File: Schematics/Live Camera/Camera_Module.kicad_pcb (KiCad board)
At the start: 2 copper layers, 69.5 x 60 mm, 90 parts, among them J1 Stack Male Edge Connector, J2 SWD_01x04_Pin, J3 USB_C_Female_USB2_Small, J4 Therm_In, J5 VTX, J6 RunCam6, J7 VTX_BATT_IN, J8 VTX_BATT_SWITCH, Q2 AO3401A, Q3 AO3400A, Q4 AO3400A, Q5 AO3401A, Q6 AO3401A, SW1 SW_STM_RESET, SW2 SW_STM_BOOT_MODE, U1 LM66100DCKR, U10 AMS1117-3.3, U11 CP2102N-Axx-xQFN28, U2 TPM8837C-SO1R, U3 STM32F103CBT6, U5 LM66100DCKR, U6 LM66100DCKR, U7 ISO1042BDWVR, U8 W25Q128JVS, Y1 X322516MMB4SI

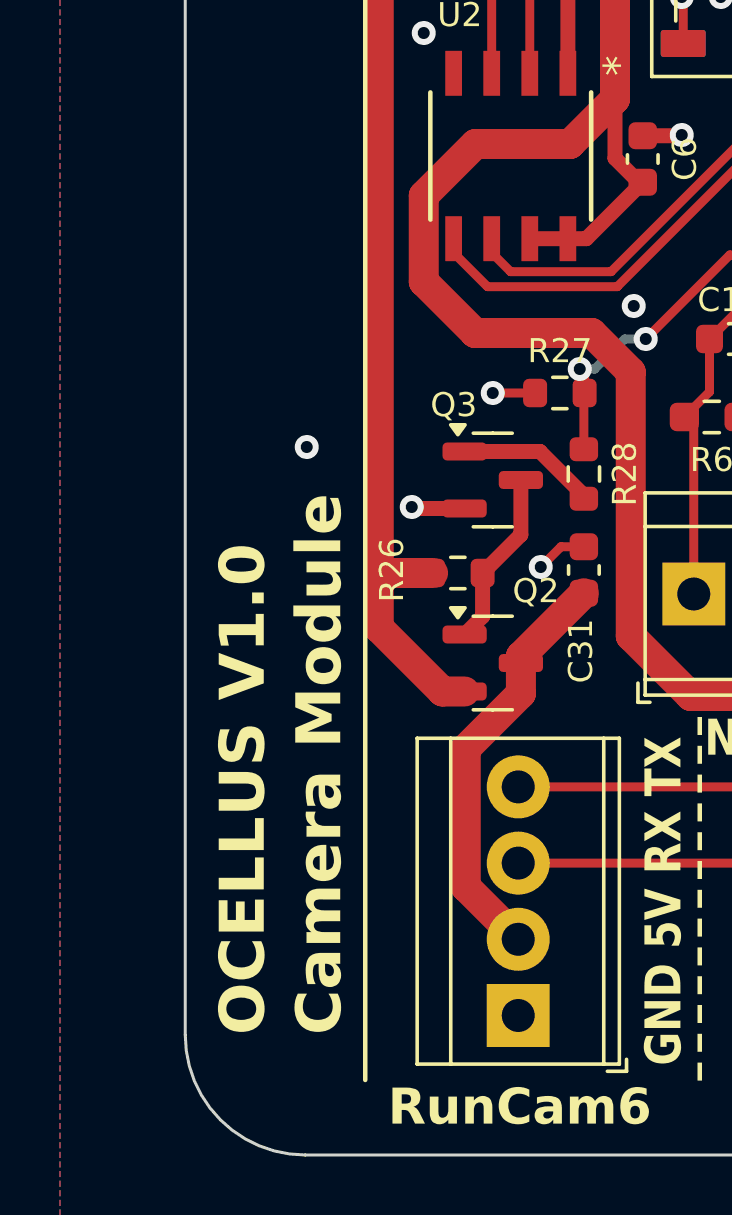
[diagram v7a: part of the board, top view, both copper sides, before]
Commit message: Final silkscreen update
Also reverted JLCPCB fields back to LCSC fields for JLCPCB export plugin purposes.
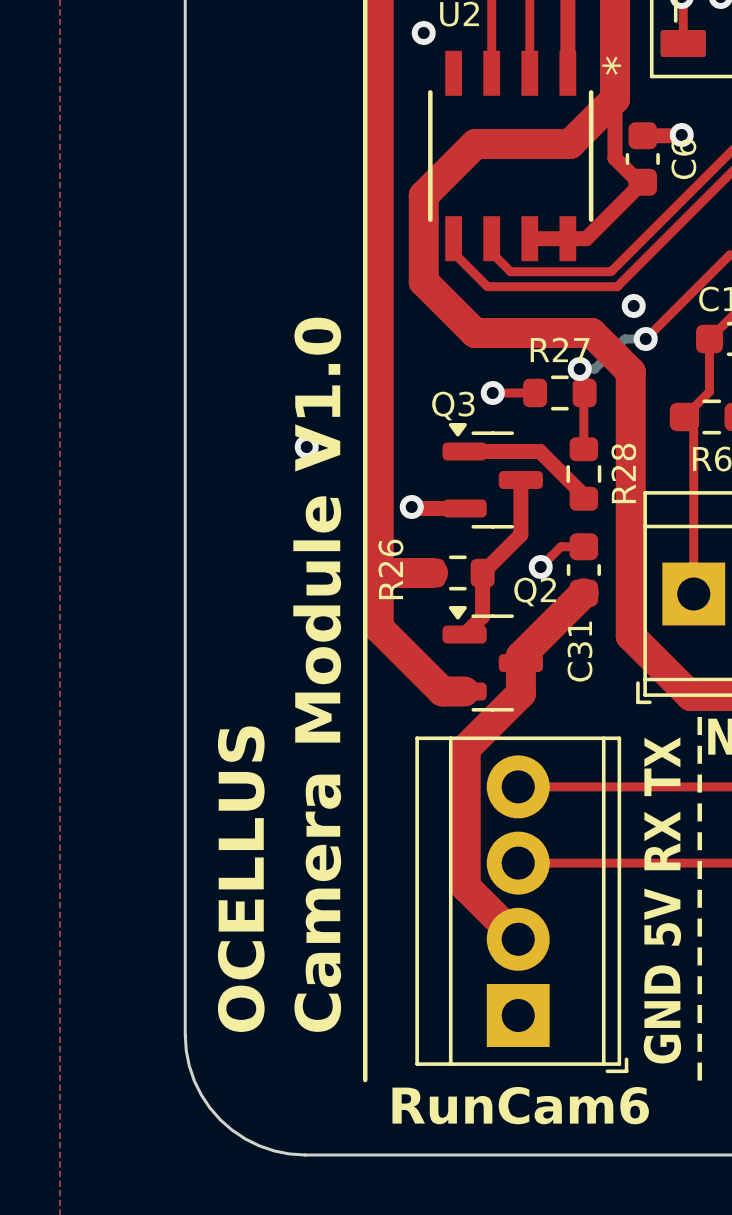
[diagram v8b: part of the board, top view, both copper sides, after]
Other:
- board text added: "Camera Module V1.0"
- board text added: "Camera Module V1.0 QRET Mar 2025 Ethan Toste Kennan Bays Noah Del Rizzo Fedor Kim"
- board text added: "OCELLUS"
- board text removed: "Camera Module"
- board text removed: "OCELLUS V1.0"
- board text removed: "Ocellus Rev 1.0 QRET Mar 2025 Ethan Toste Kennan Bays Noah Del Rizzo Fedor Kim"
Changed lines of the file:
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@@
 			(psa4output no)
 			(plotreference yes)
-			(plotvalue no)
+			(plotvalue yes)
 			(plotfptext yes)
 			(plotinvisibletext no)
@@
 		)
 	)
-	(gr_text "Ocellus Rev 1.0\nQRET Mar 2025\n\nEthan Toste\nKennan Bays\nNoah Del Rizzo\nFedor Kim"
+	(gr_text "Camera Module V1.0\nQRET Mar 2025\n\nEthan Toste\nKennan Bays\nNoah Del Rizzo\nFedor Kim"
 		(locked yes)
 		(at 121.699999 57.3 0)
@@
 		)
 	)
-	(gr_text "Camera Module"
+	(gr_text "Camera Module V1.0"
 		(at 92.3 104.099998 90)
 		(layer "F.SilkS" knockout)
@@
 		)
 	)
-	(gr_text "OCELLUS V1.0"
+	(gr_text "OCELLUS"
 		(at 89.75 104.099998 90)
 		(layer "F.SilkS" knockout)
@@
 		)
 	)
-	(group ""
-		(members "09d55dc1-6564-4b5d-9703-dd89f72fe190" "19aee215-c1fc-400f-8fc9-f98c63c16038"
-			"5041b09a-b76c-4401-aed6-59a23aec8b16" "78a48367-3922-4a98-addb-a3e61eb434ed"
-			"a36d0b29-dfe7-4db8-855c-752ecb3d3dc9" "b4493a2b-282e-4fbb-8703-64d95ebf2d98"
-			"bcd938be-cf77-47c1-b466-52b6f8f21d68" "c31124f4-edc9-4d72-aeeb-8defd2206c24"
-			"fe8ec6e2-7e09-4f9a-a208-ffe325ea4cd3"
-		)
-	)
